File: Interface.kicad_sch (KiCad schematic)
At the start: 0 parts

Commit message: changed title block to meaningful information
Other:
- title: (none) -> Open Nano Amp Meter
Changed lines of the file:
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@@
 (kicad_sch (version 20211123) (generator eeschema)
   (paper "A4")
+  (title_block
+    (title "Open Nano Amp Meter")
+    (date "2022-11-17")
+    (rev "0.9")
+  )
   (text "For transmitting the data, a well defined highly isolated interface is needed.\nThe reason for the isolated interface is the fact, that this measurement device\nshould be able to be operated at a high voltage supply. \nFor this the isolation distance of 6kV is assumed. For class B2, this results \nin 30mm, which is also assumed to be on the very safe side for using on this \nPCB."
     (at 179.07 161.29 0)

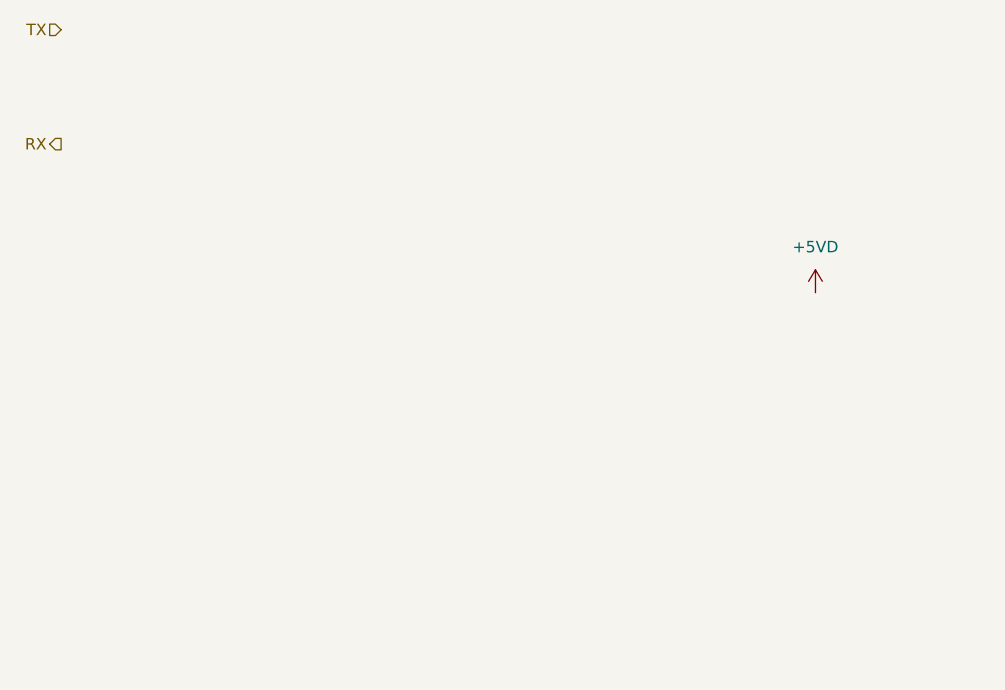
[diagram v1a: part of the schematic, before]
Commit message: added TOSLINK RX & TX
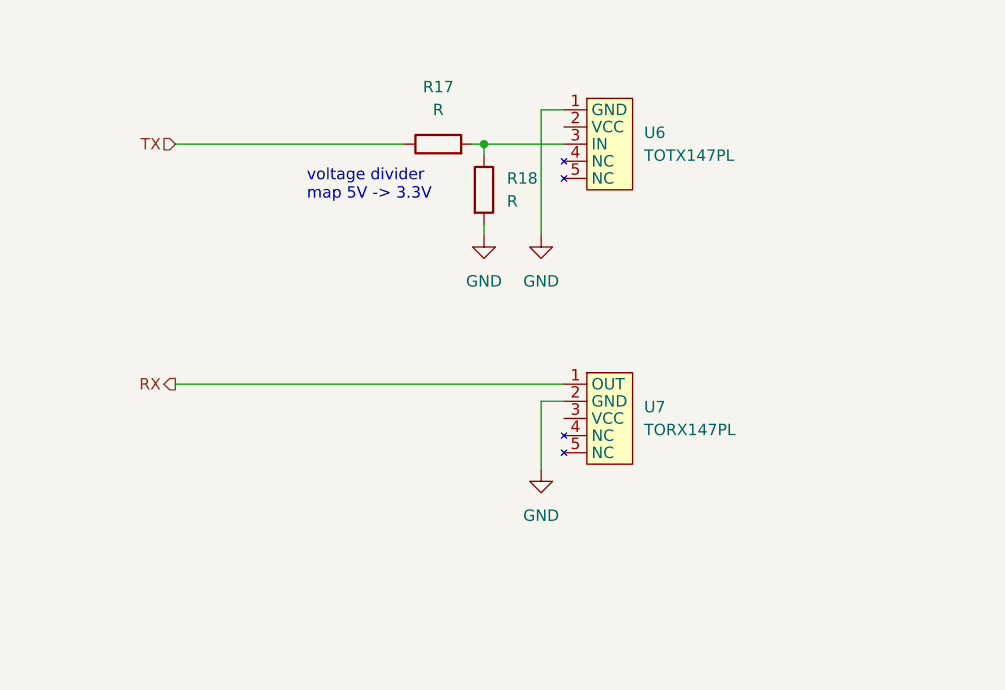
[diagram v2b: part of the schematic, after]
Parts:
- added R17, R18: R, Resistor_SMD:R_0603_1608Metric, symbol Device:R
- added U6: TOTX147PL, toslink:TOTX147PL, symbol TO_X147PL:TOTX147PL
- added U7: TORX147PL, toslink:TORX147PL, symbol TO_X147PL:TORX147PL
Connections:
- net RX: now also U7.1 (OUT)
- net TX: now also R17.1
- new net: R17.2, R18.1, U6.3 (IN)
- new net GND: R18.2, U6.1 (GND), U7.2 (GND)
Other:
- note added: "voltage divider map 5V -> 3.3V"
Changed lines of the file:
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@@
     (rev "0.9")
+  )
+  (junction (at 97.79 50.8) (diameter 0) (color 0 0 0 0)
+  )
+  (wire (pts (xy 104.14 46.99) (xy 104.14 60.96))
+    (stroke (width 0) (type default) (color 0 0 0 0))
+  )
+  (wire (pts (xy 106.68 79.375) (xy 104.14 79.375))
+    (stroke (width 0) (type default) (color 0 0 0 0))
+  )
+  (wire (pts (xy 63.5 50.8) (xy 88.9 50.8))
+    (stroke (width 0) (type default) (color 0 0 0 0))
+  )
+  (wire (pts (xy 106.68 46.99) (xy 104.14 46.99))
+    (stroke (width 0) (type default) (color 0 0 0 0))
+  )
+  (wire (pts (xy 63.5 77.47) (xy 106.68 77.47))
+    (stroke (width 0) (type default) (color 0 0 0 0))
+  )
+  (wire (pts (xy 96.52 50.8) (xy 97.79 50.8))
+    (stroke (width 0) (type default) (color 0 0 0 0))
+  )
+  (wire (pts (xy 97.79 50.8) (xy 97.79 52.07))
+    (stroke (width 0) (type default) (color 0 0 0 0))
+  )
+  (wire (pts (xy 97.79 50.8) (xy 106.68 50.8))
+    (stroke (width 0) (type default) (color 0 0 0 0))
+  )
+  (wire (pts (xy 97.79 59.69) (xy 97.79 60.96))
+    (stroke (width 0) (type default) (color 0 0 0 0))
+  )
+  (wire (pts (xy 104.14 79.375) (xy 104.14 86.995))
+    (stroke (width 0) (type default) (color 0 0 0 0))
+  )
+  (text "voltage divider\nmap 5V -> 3.3V" (at 78.105 57.15 0)
+    (effects (font (size 1.27 1.27)) (justify left bottom))
   )
   (text "For transmitting the data, a well defined highly isolated interface is needed.\nThe reason for the isolated interface is the fact, that this measurement device\nshould be able to be operated at a high voltage supply. \nFor this the isolation distance of 6kV is assumed. For class B2, this results \nin 30mm, which is also assumed to be on the very safe side for using on this \nPCB."
@@
     (effects (font (size 1.6 1.6)) (justify left bottom))
   )
-  (hierarchical_label "TX" (shape input) (at 50.8 38.1 180)
+  (hierarchical_label "TX" (shape input) (at 63.5 50.8 180)
     (effects (font (size 1.27 1.27)) (justify right))
   )
-  (hierarchical_label "RX" (shape output) (at 50.8 50.8 180)
+  (hierarchical_label "RX" (shape output) (at 63.5 77.47 180)
     (effects (font (size 1.27 1.27)) (justify right))
   )
-  (symbol (lib_id "power:+5VD") (at 134.62 67.31 0) (unit 1)
+  (symbol (lib_id "power:GND") (at 104.14 86.995 0) (unit 1)
     (in_bom yes) (on_board yes) (fields_autoplaced)
-    (property "Reference" "#PWR0111" (id 0) (at 134.62 71.12 0)
+    (property "Reference" "#PWR041" (id 0) (at 104.14 93.345 0)
       (effects (font (size 1.27 1.27)) hide)
     )
-    (property "Value" "+5VD" (id 1) (at 134.62 62.23 0))
-    (property "Footprint" "" (id 2) (at 134.62 67.31 0)
+    (property "Value" "GND" (id 1) (at 104.14 92.075 0))
+    (property "Footprint" "" (id 2) (at 104.14 86.995 0)
       (effects (font (size 1.27 1.27)) hide)
     )
-    (property "Datasheet" "" (id 3) (at 134.62 67.31 0)
+    (property "Datasheet" "" (id 3) (at 104.14 86.995 0)
       (effects (font (size 1.27 1.27)) hide)
     )
     (pin "1")
   )
+  (symbol (lib_id "Device:R") (at 97.79 55.88 0) (unit 1)
+    (in_bom yes) (on_board yes) (fields_autoplaced)
+    (property "Reference" "R18" (id 0) (at 100.33 54.6099 0)
+      (effects (font (size 1.27 1.27)) (justify left))
+    )
+    (property "Value" "R" (id 1) (at 100.33 57.1499 0)
+      (effects (font (size 1.27 1.27)) (justify left))
+    )
+    (property "Footprint" "Resistor_SMD:R_0603_1608Metric" (id 2) (at 96.012 55.88 90)
+      (effects (font (size 1.27 1.27)) hide)
+    )
+    (property "Datasheet" "~" (id 3) (at 97.79 55.88 0)
+      (effects (font (size 1.27 1.27)) hide)
+    )
+    (pin "1")
+    (pin "2")
+  )
+  (symbol (lib_id "power:GND") (at 104.14 60.96 0) (unit 1)
+    (in_bom yes) (on_board yes) (fields_autoplaced)
+    (property "Reference" "#PWR040" (id 0) (at 104.14 67.31 0)
+      (effects (font (size 1.27 1.27)) hide)
+    )
+    (property "Value" "GND" (id 1) (at 104.14 66.04 0))
+    (property "Footprint" "" (id 2) (at 104.14 60.96 0)
+      (effects (font (size 1.27 1.27)) hide)
+    )
+    (property "Datasheet" "" (id 3) (at 104.14 60.96 0)
+      (effects (font (size 1.27 1.27)) hide)
+    )
+    (pin "1")
+  )
+  (symbol (lib_id "power:GND") (at 97.79 60.96 0) (unit 1)
+    (in_bom yes) (on_board yes) (fields_autoplaced)
+    (property "Reference" "#PWR039" (id 0) (at 97.79 67.31 0)
+      (effects (font (size 1.27 1.27)) hide)
+    )
+    (property "Value" "GND" (id 1) (at 97.79 66.04 0))
+    (property "Footprint" "" (id 2) (at 97.79 60.96 0)
+      (effects (font (size 1.27 1.27)) hide)
+    )
+    (property "Datasheet" "" (id 3) (at 97.79 60.96 0)
+      (effects (font (size 1.27 1.27)) hide)
+    )
+    (pin "1")
+  )
+  (symbol (lib_id "Device:R") (at 92.71 50.8 90) (unit 1)
+    (in_bom yes) (on_board yes) (fields_autoplaced)
+    (property "Reference" "R17" (id 0) (at 92.71 44.45 90))
+    (property "Value" "R" (id 1) (at 92.71 46.99 90))
+    (property "Footprint" "Resistor_SMD:R_0603_1608Metric" (id 2) (at 92.71 52.578 90)
+      (effects (font (size 1.27 1.27)) hide)
+    )
+    (property "Datasheet" "~" (id 3) (at 92.71 50.8 0)
+      (effects (font (size 1.27 1.27)) hide)
+    )
+    (pin "1")
+    (pin "2")
+  )
+  (symbol (lib_id "TO_X147PL:TORX147PL") (at 106.68 79.375 0) (unit 1)
+    (in_bom yes) (on_board yes) (fields_autoplaced)
+    (property "Reference" "U7" (id 0) (at 115.57 80.0099 0)
+      (effects (font (size 1.27 1.27)) (justify left))
+    )
+    (property "Value" "TORX147PL" (id 1) (at 115.57 82.5499 0)
+      (effects (font (size 1.27 1.27)) (justify left))
+    )
+    (property "Footprint" "toslink:TORX147PL" (id 2) (at 106.68 79.375 0)
+      (effects (font (size 1.27 1.27)) hide)
+    )
+    (property "Datasheet" "" (id 3) (at 106.68 79.375 0)
+      (effects (font (size 1.27 1.27)) hide)
+    )
+    (pin "1")
+    (pin "2")
+    (pin "3")
+    (pin "4")
+    (pin "5")
+  )
+  (symbol (lib_id "TO_X147PL:TOTX147PL") (at 106.68 48.895 0) (unit 1)
+    (in_bom yes) (on_board yes) (fields_autoplaced)
+    (property "Reference" "U6" (id 0) (at 115.57 49.5299 0)
+      (effects (font (size 1.27 1.27)) (justify left))
+    )
+    (property "Value" "TOTX147PL" (id 1) (at 115.57 52.0699 0)
+      (effects (font (size 1.27 1.27)) (justify left))
+    )
+    (property "Footprint" "toslink:TOTX147PL" (id 2) (at 106.68 48.895 0)
+      (effects (font (size 1.27 1.27)) hide)
+    )
+    (property "Datasheet" "" (id 3) (at 106.68 48.895 0)
+      (effects (font (size 1.27 1.27)) hide)
+    )
+    (pin "1")
+    (pin "2")
+    (pin "3")
+    (pin "4")
+    (pin "5")
+  )
 )

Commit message: added 100nF decoupling and global 3V3 net
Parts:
- added C20, C21: 100n, Capacitor_SMD:C_0603_1608Metric, symbol Device:C
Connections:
- net GND: now also C20.2, C21.2
- net +3V3: now reaches U7.3 (VCC)
- net +3V3: now also U6.2 (VCC), C20.1, C21.1
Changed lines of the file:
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@@
   (junction (at 97.79 50.8) (diameter 0) (color 0 0 0 0)
   )
+  (wire (pts (xy 136.525 49.53) (xy 136.525 50.8))
+    (stroke (width 0) (type default) (color 0 0 0 0))
+  )
   (wire (pts (xy 104.14 46.99) (xy 104.14 60.96))
     (stroke (width 0) (type default) (color 0 0 0 0))
   )
+  (wire (pts (xy 106.68 48.895) (xy 105.41 48.895))
+    (stroke (width 0) (type default) (color 0 0 0 0))
+  )
   (wire (pts (xy 106.68 79.375) (xy 104.14 79.375))
     (stroke (width 0) (type default) (color 0 0 0 0))
@@
     (stroke (width 0) (type default) (color 0 0 0 0))
   )
+  (wire (pts (xy 137.16 76.2) (xy 137.16 77.47))
+    (stroke (width 0) (type default) (color 0 0 0 0))
+  )
+  (wire (pts (xy 137.16 85.09) (xy 137.16 86.36))
+    (stroke (width 0) (type default) (color 0 0 0 0))
+  )
+  (wire (pts (xy 106.68 81.28) (xy 105.41 81.28))
+    (stroke (width 0) (type default) (color 0 0 0 0))
+  )
   (wire (pts (xy 106.68 46.99) (xy 104.14 46.99))
     (stroke (width 0) (type default) (color 0 0 0 0))
   )
+  (wire (pts (xy 105.41 74.93) (xy 105.41 81.28))
+    (stroke (width 0) (type default) (color 0 0 0 0))
+  )
   (wire (pts (xy 63.5 77.47) (xy 106.68 77.47))
     (stroke (width 0) (type default) (color 0 0 0 0))
@@
     (stroke (width 0) (type default) (color 0 0 0 0))
   )
+  (wire (pts (xy 136.525 40.64) (xy 136.525 41.91))
+    (stroke (width 0) (type default) (color 0 0 0 0))
+  )
   (wire (pts (xy 97.79 59.69) (xy 97.79 60.96))
     (stroke (width 0) (type default) (color 0 0 0 0))
   )
   (wire (pts (xy 104.14 79.375) (xy 104.14 86.995))
+    (stroke (width 0) (type default) (color 0 0 0 0))
+  )
+  (wire (pts (xy 105.41 48.895) (xy 105.41 43.18))
     (stroke (width 0) (type default) (color 0 0 0 0))
   )
@@
     (pin "2")
   )
+  (symbol (lib_id "power:+3V3") (at 136.525 40.64 0) (unit 1)
+    (in_bom yes) (on_board yes) (fields_autoplaced)
+    (property "Reference" "#PWR043" (id 0) (at 136.525 44.45 0)
+      (effects (font (size 1.27 1.27)) hide)
+    )
+    (property "Value" "+3V3" (id 1) (at 136.525 35.56 0))
+    (property "Footprint" "" (id 2) (at 136.525 40.64 0)
+      (effects (font (size 1.27 1.27)) hide)
+    )
+    (property "Datasheet" "" (id 3) (at 136.525 40.64 0)
+      (effects (font (size 1.27 1.27)) hide)
+    )
+    (pin "1")
+  )
+  (symbol (lib_id "power:GND") (at 137.16 86.36 0) (unit 1)
+    (in_bom yes) (on_board yes) (fields_autoplaced)
+    (property "Reference" "#PWR046" (id 0) (at 137.16 92.71 0)
+      (effects (font (size 1.27 1.27)) hide)
+    )
+    (property "Value" "GND" (id 1) (at 137.16 91.44 0))
+    (property "Footprint" "" (id 2) (at 137.16 86.36 0)
+      (effects (font (size 1.27 1.27)) hide)
+    )
+    (property "Datasheet" "" (id 3) (at 137.16 86.36 0)
+      (effects (font (size 1.27 1.27)) hide)
+    )
+    (pin "1")
+  )
+  (symbol (lib_id "Device:C") (at 136.525 45.72 0) (unit 1)
+    (in_bom yes) (on_board yes) (fields_autoplaced)
+    (property "Reference" "C20" (id 0) (at 140.335 44.4499 0)
+      (effects (font (size 1.27 1.27)) (justify left))
+    )
+    (property "Value" "100n" (id 1) (at 140.335 46.9899 0)
+      (effects (font (size 1.27 1.27)) (justify left))
+    )
+    (property "Footprint" "Capacitor_SMD:C_0603_1608Metric" (id 2) (at 137.4902 49.53 0)
+      (effects (font (size 1.27 1.27)) hide)
+    )
+    (property "Datasheet" "~" (id 3) (at 136.525 45.72 0)
+      (effects (font (size 1.27 1.27)) hide)
+    )
+    (pin "1")
+    (pin "2")
+  )
+  (symbol (lib_id "power:+3V3") (at 105.41 74.93 0) (unit 1)
+    (in_bom yes) (on_board yes) (fields_autoplaced)
+    (property "Reference" "#PWR0111" (id 0) (at 105.41 78.74 0)
+      (effects (font (size 1.27 1.27)) hide)
+    )
+    (property "Value" "+3V3" (id 1) (at 105.41 69.85 0))
+    (property "Footprint" "" (id 2) (at 105.41 74.93 0)
+      (effects (font (size 1.27 1.27)) hide)
+    )
+    (property "Datasheet" "" (id 3) (at 105.41 74.93 0)
+      (effects (font (size 1.27 1.27)) hide)
+    )
+    (pin "1")
+  )
   (symbol (lib_id "power:GND") (at 104.14 60.96 0) (unit 1)
     (in_bom yes) (on_board yes) (fields_autoplaced)
@@
     )
     (property "Datasheet" "" (id 3) (at 104.14 60.96 0)
+      (effects (font (size 1.27 1.27)) hide)
+    )
+    (pin "1")
+  )
+  (symbol (lib_id "power:+3V3") (at 137.16 76.2 0) (unit 1)
+    (in_bom yes) (on_board yes) (fields_autoplaced)
+    (property "Reference" "#PWR045" (id 0) (at 137.16 80.01 0)
+      (effects (font (size 1.27 1.27)) hide)
+    )
+    (property "Value" "+3V3" (id 1) (at 137.16 71.12 0))
+    (property "Footprint" "" (id 2) (at 137.16 76.2 0)
+      (effects (font (size 1.27 1.27)) hide)
+    )
+    (property "Datasheet" "" (id 3) (at 137.16 76.2 0)
+      (effects (font (size 1.27 1.27)) hide)
+    )
+    (pin "1")
+  )
+  (symbol (lib_id "power:GND") (at 136.525 50.8 0) (unit 1)
+    (in_bom yes) (on_board yes) (fields_autoplaced)
+    (property "Reference" "#PWR044" (id 0) (at 136.525 57.15 0)
+      (effects (font (size 1.27 1.27)) hide)
+    )
+    (property "Value" "GND" (id 1) (at 136.525 55.88 0))
+    (property "Footprint" "" (id 2) (at 136.525 50.8 0)
+      (effects (font (size 1.27 1.27)) hide)
+    )
+    (property "Datasheet" "" (id 3) (at 136.525 50.8 0)
+      (effects (font (size 1.27 1.27)) hide)
+    )
+    (pin "1")
+  )
+  (symbol (lib_id "power:+3V3") (at 105.41 43.18 0) (unit 1)
+    (in_bom yes) (on_board yes) (fields_autoplaced)
+    (property "Reference" "#PWR0118" (id 0) (at 105.41 46.99 0)
+      (effects (font (size 1.27 1.27)) hide)
+    )
+    (property "Value" "+3V3" (id 1) (at 105.41 38.1 0))
+    (property "Footprint" "" (id 2) (at 105.41 43.18 0)
+      (effects (font (size 1.27 1.27)) hide)
+    )
+    (property "Datasheet" "" (id 3) (at 105.41 43.18 0)
       (effects (font (size 1.27 1.27)) hide)
     )
@@
     (pin "5")
   )
+  (symbol (lib_id "Device:C") (at 137.16 81.28 0) (unit 1)
+    (in_bom yes) (on_board yes) (fields_autoplaced)
+    (property "Reference" "C21" (id 0) (at 140.97 80.0099 0)
+      (effects (font (size 1.27 1.27)) (justify left))
+    )
+    (property "Value" "100n" (id 1) (at 140.97 82.5499 0)
+      (effects (font (size 1.27 1.27)) (justify left))
+    )
+    (property "Footprint" "Capacitor_SMD:C_0603_1608Metric" (id 2) (at 138.1252 85.09 0)
+      (effects (font (size 1.27 1.27)) hide)
+    )
+    (property "Datasheet" "~" (id 3) (at 137.16 81.28 0)
+      (effects (font (size 1.27 1.27)) hide)
+    )
+    (pin "1")
+    (pin "2")
+  )
 )
